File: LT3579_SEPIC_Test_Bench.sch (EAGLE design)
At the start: 121 parts

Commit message: Added new componants to schematic and board layout
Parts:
- added C_68N_FILTER_, C_68N_FILTER_1, C_68N_FILTER_2: CEU4J2X7R1H683K125AE, SamacSys_Parts:CEU4J2X7R1H683K125AE
- added C_LDO_IN_, C_LDO_IN_1, C_LDO_IN_2: CGA3E1X7R1V105K080AC, SamacSys_Parts:CGA3E1X7R1V105K080AC
- added C_LDO_OUT_, C_LDO_OUT_1, C_LDO_OUT_2: JMK107BB7475KA-T, SamacSys_Parts:JMK107BB7475KA-T
- added C_LS_, C_LS_1, C_LS_2: CGA2B2C0G1H102J050BE, SamacSys_Parts:CGA2B2C0G1H102J050BE
- added LDO_, LDO_1, LDO_2: LDL1117S33R, SamacSys_Parts:LDL1117S33R
- added LED_, LED_1, LED_2: APTD1608LCGCK, SamacSys_Parts:APTD1608LCGCK
- added NMOS_LDO_, NMOS_LDO_1, NMOS_LDO_2: RTR025N05HZGTL, SamacSys_Parts:RTR025N05HZGTL
- added R_10K_FILTER_, R_10K_FILTER_1, R_10K_FILTER_2: AC0805DR-0710KL, AC0805DR-0710KL:AC0805DR-0710KL
- added R_20K_LED1_: ERJ-2RKF2002X, SamacSys_Parts:ERJ-2RKF2002X
- added R_5.6K_LED2_: ERA-2ARB562X, SamacSys_Parts:ERA-2ARB562X
- added R_5K_FILTER_\, R_5K_FILTER_\1, R_5K_FILTER_\2: RT1206BRD075KL, SamacSys_Parts:RT1206BRD075KL
- added R_LED_10K_1, R_LED_10K_2, R_LS_DRAIN_, R_LS_DRAIN_1, R_LS_DRAIN_2: MCS0402MD1002DE000, SamacSys_Parts:MCS0402MD1002DE000
- added R_LS_GATE_, R_LS_GATE_1, R_LS_GATE_2: AT0805FRE07100KL, AT0805FRE07100KL:AT0805FRE07100KL
- added TP_CLK_FILTER_, TP_CLK_FILTER_1, TP_CLK_FILTER_2, TP_FAULT_LS_, TP_FAULT_LS_1, TP_FAULT_LS_2, TP_LDO_OUT_, TP_LDO_OUT_1, TP_LDO_OUT_2: S1751-46R, S1751-46R:S1751-46R
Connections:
- new net CLK_FILTER_OUT_: 12P_OUTPUT_CONNECTOR1.6, C_68N_FILTER_.1, R_10K_FILTER_.2, R_5K_FILTER_\.1, TP_CLK_FILTER_.1
- new net CLK_FILTER_OUT_1: 12P_OUTPUT_CONNECTOR1.4, C_68N_FILTER_1.1, R_10K_FILTER_1.2, R_5K_FILTER_\1.1, TP_CLK_FILTER_1.1
- new net CLK_FILTER_OUT_2: 12P_OUTPUT_CONNECTOR1.2, C_68N_FILTER_2.1, R_10K_FILTER_2.2, R_5K_FILTER_\2.1, TP_CLK_FILTER_2.1
- new net FAULT_LS_OUT_: 12P_OUTPUT_CONNECTOR1.5, C_LS_.1, NMOS_LDO_.DRAIN, R_LS_DRAIN_.1, TP_FAULT_LS_.1
- new net FAULT_LS_OUT_1: 12P_OUTPUT_CONNECTOR1.3, C_LS_1.1, NMOS_LDO_1.DRAIN, R_LS_DRAIN_1.1, TP_FAULT_LS_1.1
- new net FAULT_LS_OUT_2: 12P_OUTPUT_CONNECTOR1.1, C_LS_2.1, NMOS_LDO_2.DRAIN, R_LS_DRAIN_2.1, TP_FAULT_LS_2.1
- new net LDO_OUT_: C_LDO_OUT_.1, LDO_.VOUT_1, LDO_.VOUT_2, R_LS_DRAIN_.2, TP_LDO_OUT_.1
- new net LDO_OUT_1: C_LDO_OUT_1.1, LDO_1.VOUT_1, LDO_1.VOUT_2, R_LS_DRAIN_1.2, TP_LDO_OUT_1.1
- new net LDO_OUT_2: C_LDO_OUT_2.1, LDO_2.VOUT_1, LDO_2.VOUT_2, R_LS_DRAIN_2.2, TP_LDO_OUT_2.1
- new net N$10: NMOS_LDO_1.GATE, R_LS_GATE_1.2
- new net N$11: LED_1.A, R_LED_10K_1.2
- new net N$12: R_20K_LED1_.1, R_5.6K_LED2_.1
- new net N$14: NMOS_LDO_2.GATE, R_LS_GATE_2.2
- new net N$15: LED_.A, R_5.6K_LED2_.2
- new net N$16: LED_2.A, R_LED_10K_2.2
- new net N$8: NMOS_LDO_.GATE, R_LS_GATE_.2
- net 0: now also C_68N_FILTER_.2, C_68N_FILTER_1.2, C_68N_FILTER_2.2, C_LDO_IN_.2, C_LDO_IN_1.2, C_LDO_IN_2.2, C_LDO_OUT_.2, C_LDO_OUT_1.2, C_LDO_OUT_2.2, C_LS_.2, C_LS_1.2, C_LS_2.2, LED_.K, LED_1.K, LED_2.K, NMOS_LDO_.SOURCE, NMOS_LDO_1.SOURCE, NMOS_LDO_2.SOURCE, R_5K_FILTER_\.2, R_5K_FILTER_\1.2, R_5K_FILTER_\2.2
- net CLK_: now also R_10K_FILTER_.1; no longer 12P_OUTPUT_CONNECTOR1.6
- net CLK_1: now also R_10K_FILTER_1.1; no longer 12P_OUTPUT_CONNECTOR1.4
- net CLK_2: now also R_10K_FILTER_2.1; no longer 12P_OUTPUT_CONNECTOR1.2
- net FAULT_: now also R_LS_GATE_.1; no longer 12P_OUTPUT_CONNECTOR1.5
- net FAULT_1: now also R_LS_GATE_1.1; no longer 12P_OUTPUT_CONNECTOR1.3
- net FAULT_2: now also R_LS_GATE_2.1; no longer 12P_OUTPUT_CONNECTOR1.1
- net GND: now also LDO_.GND, LDO_1.GND, LDO_2.GND
- net VIN: now also C_LDO_IN_.1, C_LDO_IN_1.1, C_LDO_IN_2.1, LDO_.VIN, LDO_1.VIN, LDO_2.VIN
- net VOUT_: now also R_20K_LED1_.2
- net VOUT_1: now also R_LED_10K_1.1
- net VOUT_2: now also R_LED_10K_2.1
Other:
- note added: "13V -> 3.3V output"
- note added: "13V FAULT logic level -> 3.3V Logic Level"
- note added: "20K + 5.6K Series Resistance"
- note added: "Filter to convert pulse signal to DC"
- moved on the sheet: R_SHUNT_GND_, R_SHUNT_GND_1, R_SHUNT_GND_2, TP_CH_GND_, TP_CH_GND_1, TP_CH_GND_2, TP_GND_, TP_GND_1, TP_GND_2

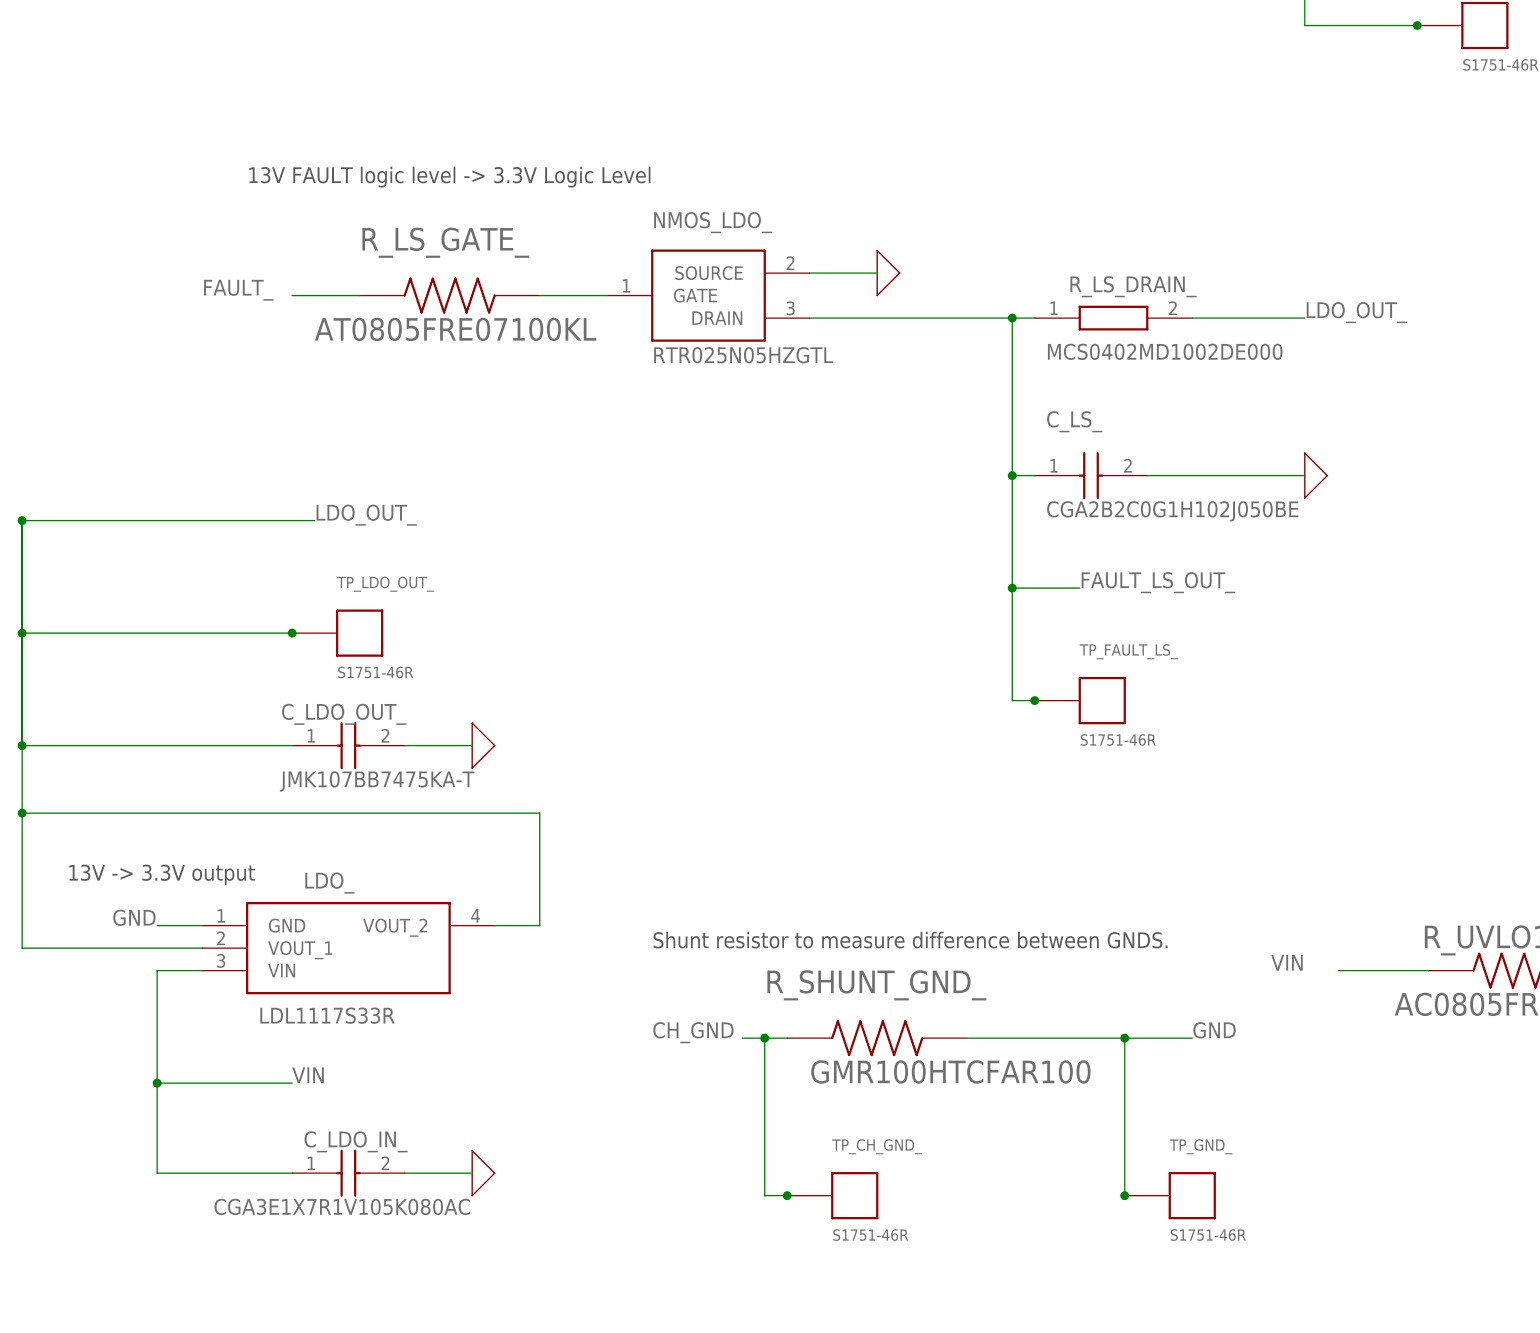
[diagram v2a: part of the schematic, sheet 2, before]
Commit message: Made board layout more compact. used more backside of board
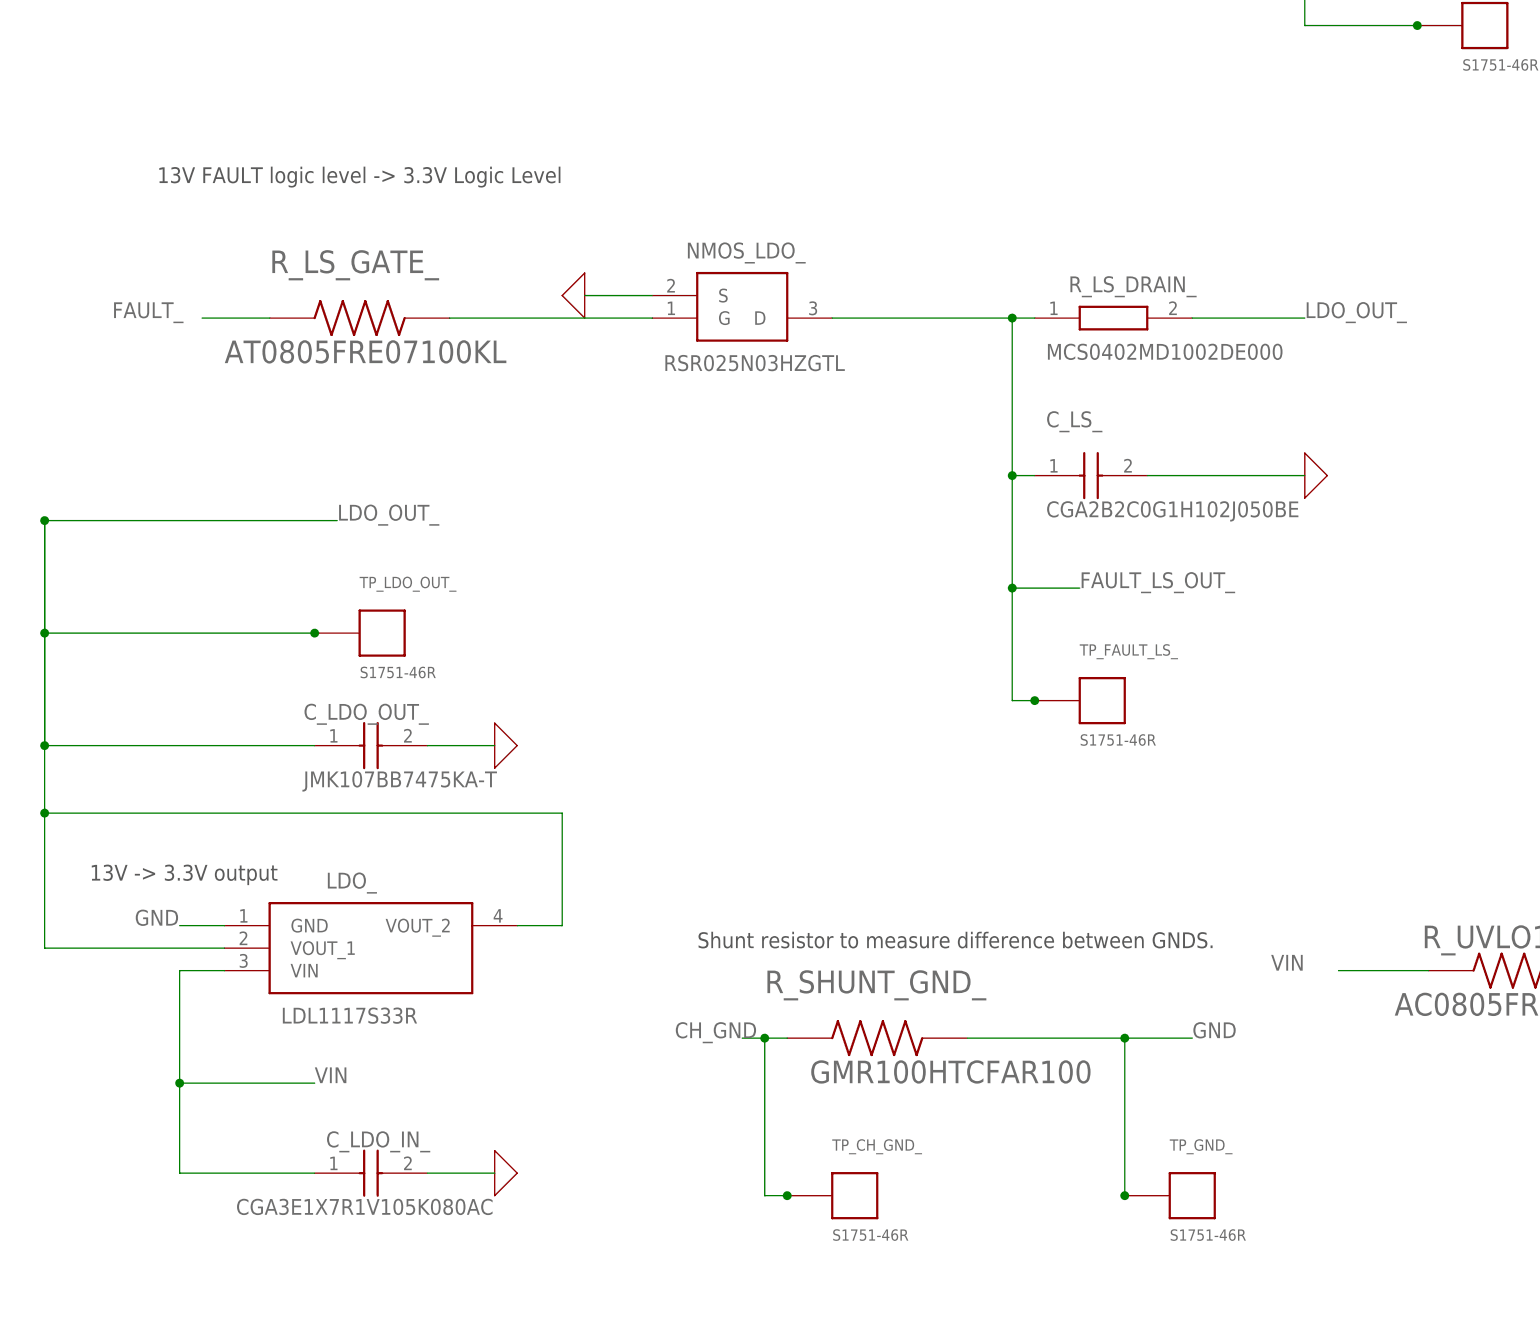
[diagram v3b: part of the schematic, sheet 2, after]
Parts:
- removed C_LDO_IN_1, C_LDO_IN_2: CGA3E1X7R1V105K080AC, SamacSys_Parts:CGA3E1X7R1V105K080AC
- removed C_LDO_OUT_1, C_LDO_OUT_2: JMK107BB7475KA-T, SamacSys_Parts:JMK107BB7475KA-T
- removed LDO_1, LDO_2: LDL1117S33R, SamacSys_Parts:LDL1117S33R
- removed TP_LDO_OUT_1, TP_LDO_OUT_2: S1751-46R, S1751-46R:S1751-46R
- NMOS_LDO_, NMOS_LDO_1, NMOS_LDO_2: value RTR025N05HZGTL -> RSR025N03HZGTL; device SamacSys_Parts:RTR025N05HZGTL -> SamacSys_Parts:RSR025N03HZGTL
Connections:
- removed net LDO_OUT_1: C_LDO_OUT_1.1, LDO_1.VOUT_1, LDO_1.VOUT_2, R_LS_DRAIN_1.2, TP_LDO_OUT_1.1
- removed net LDO_OUT_2: C_LDO_OUT_2.1, LDO_2.VOUT_1, LDO_2.VOUT_2, R_LS_DRAIN_2.2, TP_LDO_OUT_2.1
- net 0: now also NMOS_LDO_.S, NMOS_LDO_1.S, NMOS_LDO_2.S; no longer C_LDO_IN_1.2, C_LDO_IN_2.2, C_LDO_OUT_1.2, C_LDO_OUT_2.2, NMOS_LDO_.SOURCE, NMOS_LDO_1.SOURCE, NMOS_LDO_2.SOURCE
- net FAULT_LS_OUT_: now also NMOS_LDO_.D; no longer NMOS_LDO_.DRAIN
- net FAULT_LS_OUT_1: now also NMOS_LDO_1.D; no longer NMOS_LDO_1.DRAIN
- net FAULT_LS_OUT_2: now also NMOS_LDO_2.D; no longer NMOS_LDO_2.DRAIN
- net GND: no longer LDO_1.GND, LDO_2.GND
- net LDO_OUT_: now also R_LS_DRAIN_1.2, R_LS_DRAIN_2.2
- net N$10: now also NMOS_LDO_1.G; no longer NMOS_LDO_1.GATE
- net N$14: now also NMOS_LDO_2.G; no longer NMOS_LDO_2.GATE
- net N$8: now also NMOS_LDO_.G; no longer NMOS_LDO_.GATE
- net VIN: no longer C_LDO_IN_1.1, C_LDO_IN_2.1, LDO_1.VIN, LDO_2.VIN
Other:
- moved on the sheet: C_LDO_IN_, C_LDO_OUT_, LDO_, NMOS_LDO_, NMOS_LDO_1, NMOS_LDO_2, R_LS_GATE_, R_LS_GATE_1, R_LS_GATE_2, TP_LDO_OUT_
